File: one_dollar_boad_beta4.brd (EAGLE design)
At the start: 85.6 x 54 mm, 39 parts, among them IC1 ATTINY85, X1 USBPCB

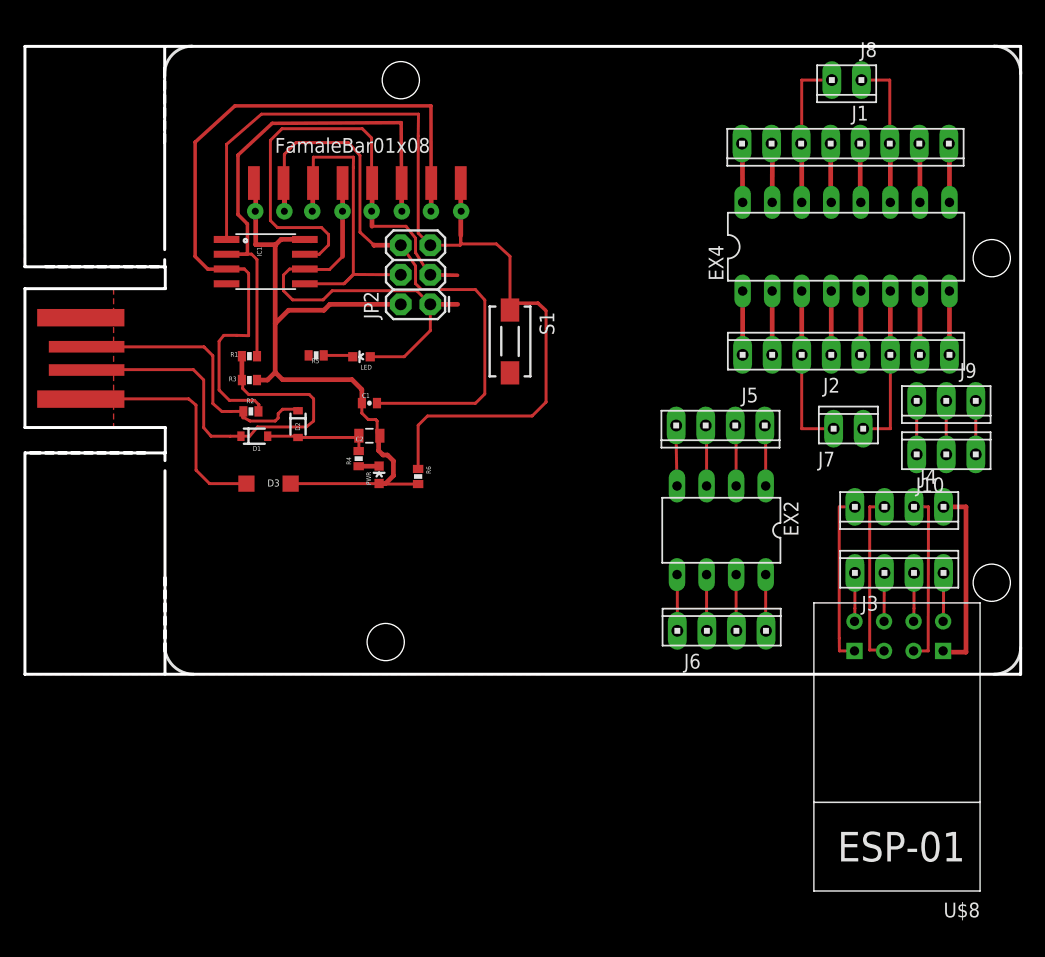
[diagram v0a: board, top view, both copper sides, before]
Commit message: Eliminado nomes de CIs
Motivo: pode confundir usuarios
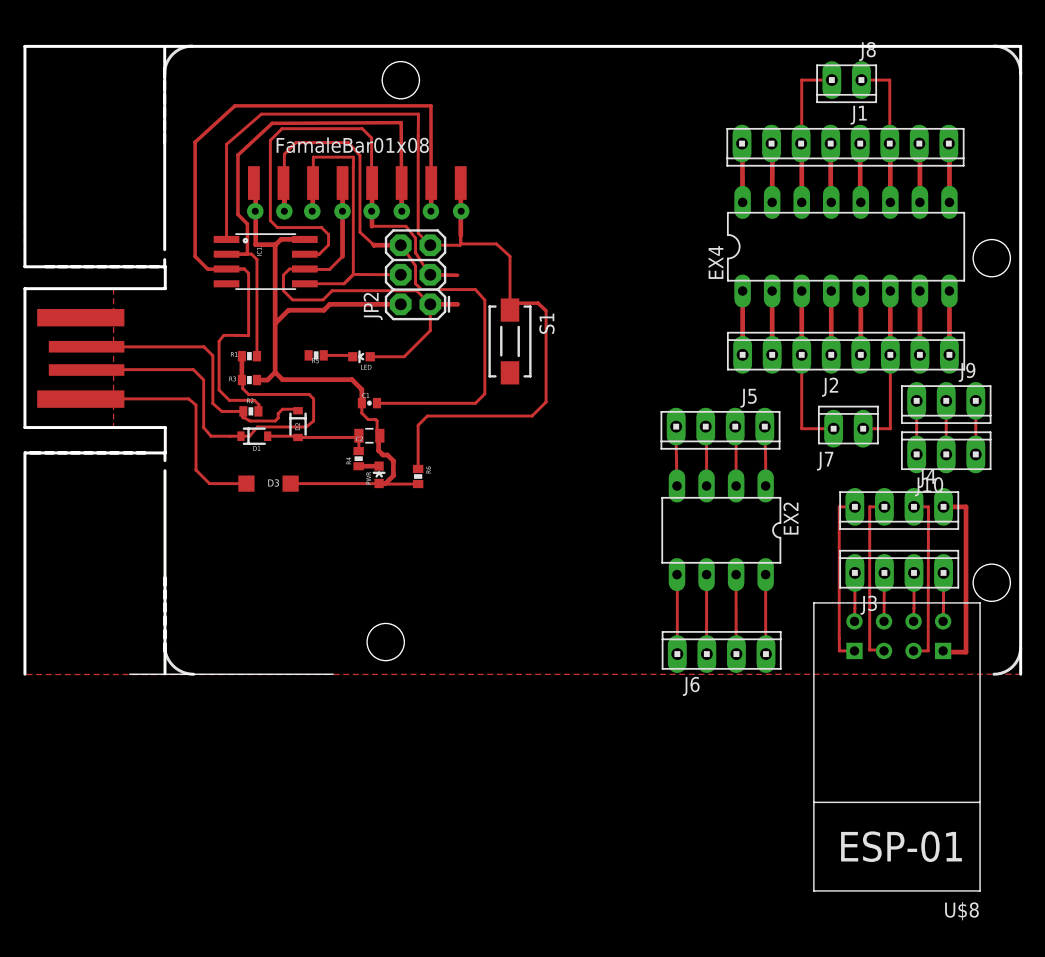
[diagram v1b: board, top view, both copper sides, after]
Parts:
- EX2: value AT24CP -> (none)
- EX4: value L293D -> (none)
- S1: value DTSM-3 -> RESET
- moved J6 2.00 mm to (59.9, 1.73)
- moved J5 0.10 mm to (59.8, 21.3)
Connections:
- net N$22 renamed EX1
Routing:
- net N$24: track 4.93 -> 6.93 mm
- net N$23: track 4.86 -> 6.83 mm
- net N$14: track 4.86 -> 6.83 mm
- net N$13: track 4.86 -> 6.83 mm
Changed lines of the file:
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@@
 <?xml version="1.0" encoding="utf-8"?>
 <!DOCTYPE eagle SYSTEM "eagle.dtd">
-<eagle version="7.5.0">
+<eagle version="6.6.0">
 <drawing>
 <settings>
@@
 <dimension x1="0" y1="0" x2="85.598" y2="0" x3="42.799" y3="-8.382" textsize="1.778" layer="20"/>
 <dimension x1="9" y1="0" x2="9" y2="19" x3="-5.334" y3="9.5" textsize="1.778" layer="20"/>
-<wire x1="85.598" y1="0" x2="0" y2="0" width="0.254" layer="20"/>
 <wire x1="0" y1="0" x2="0" y2="19.05" width="0.254" layer="20"/>
 <wire x1="12.065" y1="19.05" x2="12.065" y2="21.209" width="0.254" layer="20"/>
@@
 <text x="76" y="0.3" size="0.8128" layer="27">3</text>
 <text x="78.6" y="0.3" size="0.8128" layer="27">4</text>
-<text x="70.4" y="5.2" size="0.8128" layer="27">5</text>
 <text x="73" y="5.2" size="0.8128" layer="27">6</text>
 <text x="75.5" y="5.2" size="0.8128" layer="27">7</text>
@@
 <pass name="Default">
 <param name="RoutingGrid" value="6mil"/>
-<param name="AutoGrid" value="1"/>
-<param name="Efforts" value="0"/>
-<param name="TopRouterVariant" value="1"/>
 <param name="tpViaShape" value="round"/>
 <param name="PrefDir.1" value="|"/>
@@
 <attribute name="PROD_ID" value="CONN-09701" x="34.8488" y="31.8008" size="1.778" layer="27" rot="R90" display="off"/>
 </element>
-<element name="S1" library="switch-tact" package="DTSM-3" value="DTSM-3" x="41.6988" y="28.6098" rot="R270"/>
-<element name="EX4" library="st-microelectronics" package="DIL16" value="L293D" x="70.5866" y="36.7538">
+<element name="S1" library="switch-tact" package="DTSM-3" value="RESET" x="41.6988" y="28.6098" rot="R270"/>
+<element name="EX4" library="st-microelectronics" package="DIL16" value="" x="70.5866" y="36.7538">
 <attribute name="MF" value="" x="70.5866" y="36.7538" size="1.778" layer="27" display="off"/>
 <attribute name="MPN" value="L293D" x="70.5866" y="36.7538" size="1.778" layer="27" display="off"/>
@@
 <element name="J3" library="con-amp" package="10X04MTA" value="" x="75.1586" y="8.7122"/>
 <element name="J4" library="con-amp" package="10X04MTA" value="" x="75.157" y="14.3892" rot="R180"/>
-<element name="EX2" library="atmel" package="DIL08" value="AT24CP" x="59.8662" y="12.376" rot="R180">
+<element name="EX2" library="atmel" package="DIL08" value="" x="59.8662" y="12.376" rot="R180">
 <attribute name="MF" value="" x="59.8662" y="12.376" size="1.778" layer="27" rot="R180" display="off"/>
 <attribute name="MPN" value="AT24C1024BW-SH-B" x="59.8662" y="12.376" size="1.778" layer="27" rot="R180" display="off"/>
@@
 <attribute name="OC_NEWARK" value="03P2044" x="59.8662" y="12.376" size="1.778" layer="27" rot="R180" display="off"/>
 </element>
-<element name="J5" library="con-amp" package="10X04MTA" value="" x="59.7932" y="21.3868" rot="R180"/>
-<element name="J6" library="con-amp" package="10X04MTA" value="" x="59.8932" y="3.7338"/>
+<element name="J5" library="con-amp" package="10X04MTA" value="" x="59.7932" y="21.2868" rot="R180"/>
+<element name="J6" library="con-amp" package="10X04MTA" value="" x="59.8932" y="1.7338"/>
 <element name="J7" library="con-amp" package="10X02MTA" value="" x="70.7898" y="21.1074"/>
 <element name="J8" library="con-amp" package="10X02MTA" value="" x="70.6374" y="51.0794" rot="R180"/>
@@
 <wire x1="22.3" y1="39.8" x2="22.3" y2="39.3" width="0.4064" layer="1"/>
 <via x="22.3" y="39.8" extent="1-16" drill="0.6" diameter="1.4224"/>
-<wire x1="56.0562" y1="16.186" x2="55.9562" y2="21.2562" width="0.254" layer="1"/>
-<wire x1="55.9562" y1="21.2562" x2="56.1" y2="21.4" width="0.4064" layer="1"/>
+<wire x1="56.0562" y1="16.186" x2="55.9562" y2="21.1562" width="0.254" layer="1"/>
+<wire x1="55.9562" y1="21.1562" x2="56.1" y2="21.3" width="0.4064" layer="1"/>
 <contactref element="EX4" pad="5"/>
 <wire x1="22.3" y1="39.8" x2="22.3" y2="42.4" width="0.4064" layer="1"/>
@@
 <contactref element="J6" pad="1"/>
 <contactref element="EX2" pad="8"/>
-<wire x1="63.7032" y1="3.7338" x2="63.6778" y2="3.7338" width="0.254" layer="1"/>
+<wire x1="63.7032" y1="1.7338" x2="63.6778" y2="3.7338" width="0.254" layer="1"/>
 <wire x1="63.6778" y1="3.7338" x2="63.6762" y2="8.566" width="0.254" layer="1"/>
 </signal>
@@
 <contactref element="J6" pad="2"/>
 <contactref element="EX2" pad="7"/>
-<wire x1="61.1632" y1="3.7338" x2="61.1378" y2="3.7338" width="0.254" layer="1"/>
+<wire x1="61.1632" y1="1.7338" x2="61.1378" y2="3.7338" width="0.254" layer="1"/>
 <wire x1="61.1378" y1="3.7338" x2="61.1362" y2="8.566" width="0.254" layer="1"/>
 </signal>
@@
 <contactref element="EX2" pad="6"/>
 <contactref element="J6" pad="3"/>
-<wire x1="58.6232" y1="3.7338" x2="58.5978" y2="3.7338" width="0.254" layer="1"/>
+<wire x1="58.6232" y1="1.7338" x2="58.5978" y2="3.7338" width="0.254" layer="1"/>
 <wire x1="58.5978" y1="3.7338" x2="58.5962" y2="8.566" width="0.254" layer="1"/>
 </signal>
@@
 <contactref element="EX2" pad="5"/>
 <wire x1="56.0562" y1="8.566" x2="56.0832" y2="8.6106" width="0.254" layer="1"/>
-<wire x1="56.0832" y1="8.6106" x2="56.0832" y2="3.7338" width="0.254" layer="1"/>
+<wire x1="56.0832" y1="8.6106" x2="56.0832" y2="1.7338" width="0.254" layer="1"/>
 </signal>
 <signal name="N$28">
 <contactref element="EX2" pad="3"/>
 <contactref element="J5" pad="2"/>
-<wire x1="58.5232" y1="21.3868" x2="58.5978" y2="21.336" width="0.254" layer="1"/>
-<wire x1="58.5978" y1="21.336" x2="58.5962" y2="16.186" width="0.254" layer="1"/>
+<wire x1="58.5232" y1="21.2868" x2="58.5978" y2="21.236" width="0.254" layer="1"/>
+<wire x1="58.5978" y1="21.236" x2="58.5962" y2="16.186" width="0.254" layer="1"/>
 </signal>
 <signal name="N$36">
 <contactref element="J5" pad="3"/>
 <contactref element="EX2" pad="2"/>
-<wire x1="61.0632" y1="21.3868" x2="61.1378" y2="21.336" width="0.254" layer="1"/>
-<wire x1="61.1378" y1="21.336" x2="61.1362" y2="16.186" width="0.254" layer="1"/>
+<wire x1="61.0632" y1="21.2868" x2="61.1378" y2="21.236" width="0.254" layer="1"/>
+<wire x1="61.1378" y1="21.236" x2="61.1362" y2="16.186" width="0.254" layer="1"/>
 </signal>
 <signal name="N$37">
 <contactref element="EX2" pad="1"/>
 <contactref element="J5" pad="4"/>
-<wire x1="63.6032" y1="21.3868" x2="63.6778" y2="21.336" width="0.254" layer="1"/>
-<wire x1="63.6778" y1="21.336" x2="63.6762" y2="16.186" width="0.254" layer="1"/>
+<wire x1="63.6032" y1="21.2868" x2="63.6778" y2="18.536" width="0.254" layer="1"/>
+<wire x1="63.6778" y1="18.536" x2="63.6762" y2="16.186" width="0.254" layer="1"/>
 </signal>
 <signal name="N$7">
@@
 <wire x1="61.6712" y1="45.5422" x2="61.6458" y2="45.6184" width="0.254" layer="1"/>
 </signal>
-<signal name="N$22">
+<signal name="EX1">
 <contactref element="EX4" pad="15"/>
 <contactref element="J1" pad="2"/>

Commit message: Adicionado nome de pinos e mudança de lugar de RST
Colocado números e descrição de PINOS
Mudança de lugar de Botão RESET
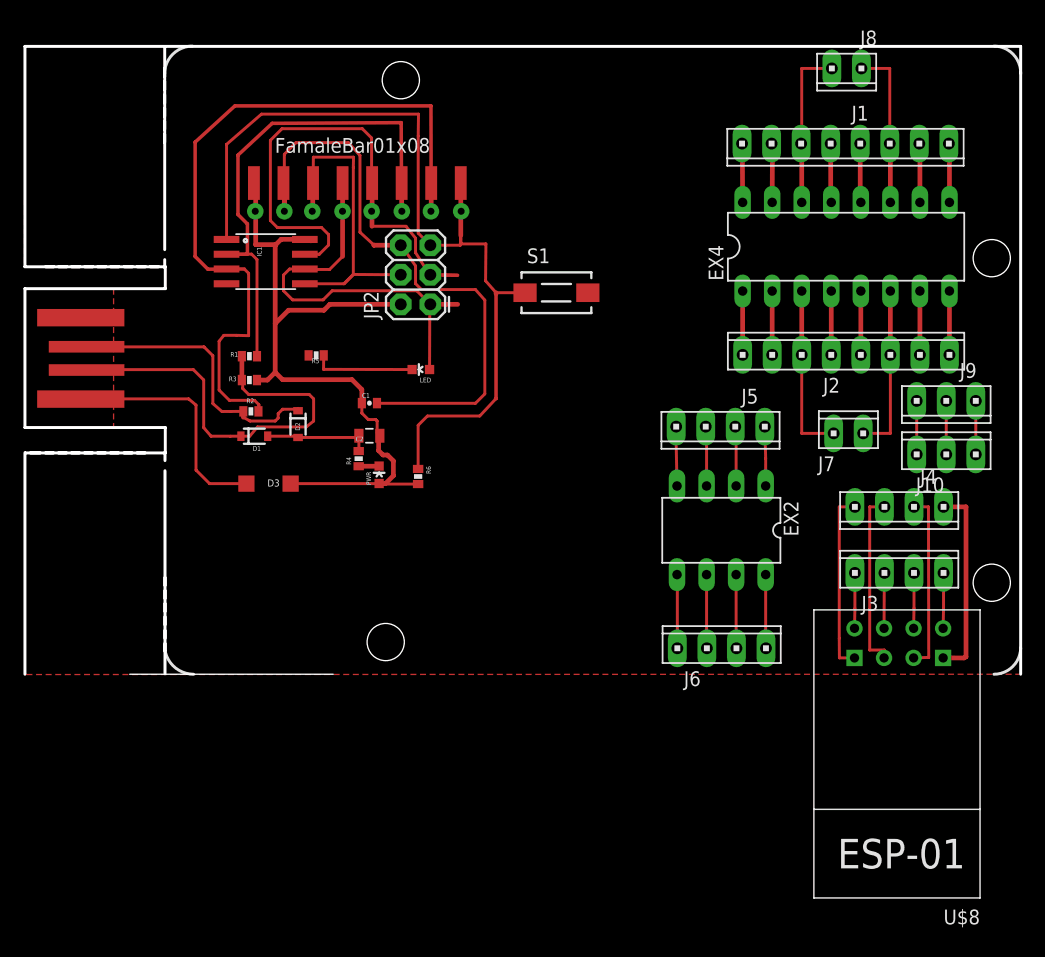
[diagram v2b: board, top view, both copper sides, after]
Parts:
- removed LOGO2: LOGO-OSHW-10MILX0200-NT, logo:OSHW_10X200_NOTEXT
- JP2: value ICSP -> (none)
- U$8: value ESP01 -> EX1
- moved S1 5.79 mm to (45.7, 32.8), turned to 0 degrees
- moved LED 5.22 mm to (34.0, 26.2)
- moved J8 1.00 mm to (70.6, 52.1)
- moved U$8 0.60 mm to (75.1, -4.23)
- moved J6 0.50 mm to (59.9, 2.23)
- moved J7 0.40 mm to (70.8, 20.7)
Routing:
- net N$12: track 2.54 -> 8.82 mm
- net N$47: track 82.1 -> 75.9 mm
- net N$3: track 35.6 -> 32.9 mm
- net N$38: track 13.0 -> 14.0 mm
- net N$25: track 13.2 -> 14.2 mm
- net N$29: track 14.9 -> 15.5 mm
- net N$34: track 4.17 -> 4.77 mm
- net N$31: track 15.0 -> 15.6 mm
- net N$33: track 4.17 -> 4.77 mm
- net N$32: track 4.17 -> 4.77 mm
- net N$35: track 4.17 -> 4.77 mm
- net N$30: track 14.9 -> 15.5 mm
- net N$24: track 6.93 -> 6.43 mm
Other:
- board text added: "10"
- board text added: "11"
- board text added: "12"
- board text added: "13"
- board text added: "14"
- board text added: "15"
- board text added: "16"
- board text added: "2 D-"
- board text added: "3 D+"
- board text added: "4 GND"
- board text added: "5V"
- board text added: "9"
- board text added: "EX3"
- board text added: "GND"
- board text added: "ISP"
- board text added: "M1"
- board text added: "M2"
- board text added: "MBR0520LT"
- board text added: "ONE DOLLAR BOARD BETA 4 Please download last version: https://github.com/Onedollarboard/PCB"
- board text added: "POWER LED"
- board text added: "VCC +5V"
- board text removed: "Based on project by Erik Kettenbugr, Digistump LLC - digistump.com 2012, Modified by Thalis Antunes at the request of Claudio Olmedo"
